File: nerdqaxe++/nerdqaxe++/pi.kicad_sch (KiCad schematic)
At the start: 20 parts, among them J5 Conn_01x12-Socket, J6 Conn_01x12-Socket, J7 Conn_01x12-Header, J8 Conn_01x12-Header, M1 Fan_4pin, M2 Fan_4pin, U30 T-Display-S3, U32 EMC2302-1, U33 TXU0102-DCU, U37 TMP1075, U38 TMP1075

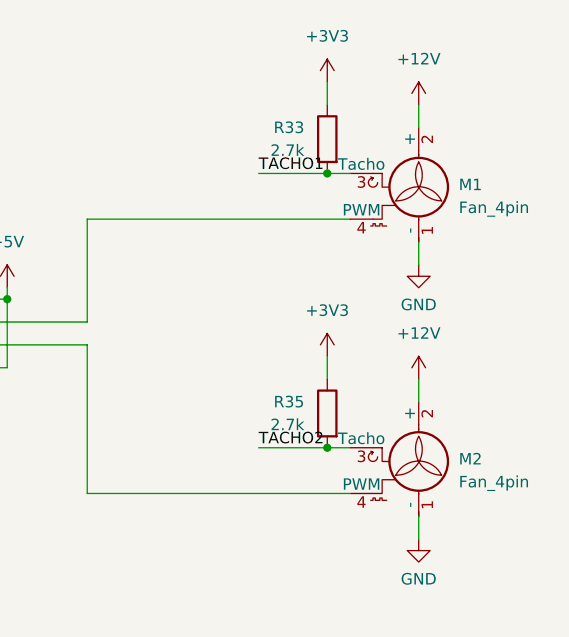
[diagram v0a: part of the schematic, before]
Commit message: removed solderjumpers on ++
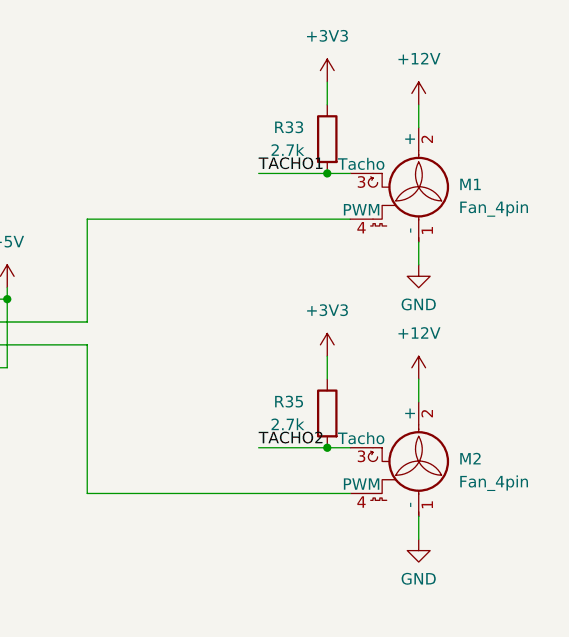
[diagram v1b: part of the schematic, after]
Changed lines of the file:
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@@
 (kicad_sch
-	(version 20231120)
+	(version 20250114)
 	(generator "eeschema")
-	(generator_version "8.0")
+	(generator_version "9.0")
 	(paper "A4")
+	(text "1x12 Socket for NerdQaxe+"
+		(exclude_from_sim no)
+		(at 29.21 179.07 0)
+		(effects
+			(font
+				(size 1.27 1.27)
+			)
+		)
+	)
+	(text "1x12 Pinheader for T-Display-S3"
+		(exclude_from_sim no)
+		(at 61.595 179.07 0)
+		(effects
+			(font
+				(size 1.27 1.27)
+			)
+		)
+	)
 	(junction
 		(at 220.345 131.445)
@@
 		)
 	)
-	(text "1x12 Socket for NerdQaxe+"
-		(exclude_from_sim no)
-		(at 29.21 179.07 0)
-		(effects
-			(font
-				(size 1.27 1.27)
-			)
-		)
-	)
-	(text "1x12 Pinheader for T-Display-S3"
-		(exclude_from_sim no)
-		(at 61.595 179.07 0)
-		(effects
-			(font
-				(size 1.27 1.27)
-			)
-		)
-	)
 	(label "SCL"
 		(at 201.295 53.975 0)
-		(fields_autoplaced yes)
 		(effects
 			(font
@@
 	(label "SDA"
 		(at 248.285 53.975 180)
-		(fields_autoplaced yes)
 		(effects
 			(font
@@
 	(label "SDA"
 		(at 139.065 128.905 180)
-		(fields_autoplaced yes)
 		(effects
 			(font
@@
 	(label "SCL"
 		(at 139.065 131.445 180)
-		(fields_autoplaced yes)
 		(effects
 			(font
@@
 	(label "TACHO1"
 		(at 174.625 139.065 0)
-		(fields_autoplaced yes)
 		(effects
 			(font
@@
 	(label "TACHO2"
 		(at 174.625 133.985 0)
-		(fields_autoplaced yes)
 		(effects
 			(font
@@
 	(label "TACHO2"
 		(at 248.285 147.955 0)
-		(fields_autoplaced yes)
 		(effects
 			(font
@@
 	(label "TACHO1"
 		(at 248.285 117.475 0)
-		(fields_autoplaced yes)
 		(effects
 			(font
@@
 		(shape bidirectional)
 		(at 154.305 76.835 0)
-		(fields_autoplaced yes)
 		(effects
 			(font
@@
 		(shape input)
 		(at 57.785 18.415 180)
-		(fields_autoplaced yes)
 		(effects
 			(font
@@
 		(shape output)
 		(at 97.79 79.375 180)
-		(fields_autoplaced yes)
 		(effects
 			(font
@@
 		(shape input)
 		(at 154.305 79.375 0)
-		(fields_autoplaced yes)
 		(effects
 			(font
@@
 		(shape input)
 		(at 103.505 99.695 180)
-		(fields_autoplaced yes)
 		(effects
 			(font
@@
 		(shape output)
 		(at 57.785 23.495 180)
-		(fields_autoplaced yes)
 		(effects
 			(font
@@
 		(shape output)
 		(at 154.305 74.295 0)
-		(fields_autoplaced yes)
 		(effects
 			(font
@@
 		(shape output)
 		(at 113.665 71.755 180)
-		(fields_autoplaced yes)
 		(effects
 			(font
@@
 		(shape input)
 		(at 57.785 20.955 180)
-		(fields_autoplaced yes)
 		(effects
 			(font
@@
 		(shape output)
 		(at 154.305 81.915 0)
-		(fields_autoplaced yes)
 		(effects
 			(font
@@
 		(shape output)
 		(at 110.49 86.995 180)
-		(fields_autoplaced yes)
 		(effects
 			(font
@@
 		(shape input)
 		(at 80.645 81.915 180)
-		(fields_autoplaced yes)
 		(effects
 			(font
@@
 		)
 	)
+	(embedded_fonts no)
 )

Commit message: rev5.1.1
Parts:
- added R16: 10k, Resistor_SMD:R_0805_2012Metric, symbol Device:R
- added R8, R9: 3.3k, Resistor_SMD:R_0805_2012Metric, symbol Device:R
- C102, C103, C87, C88, C96: Distributor (none) -> D; Manufacturer (none) -> C0805C104K5RACTU; OrderNr (none) -> 399-C0805C104K5RACTUCT-ND; temp-coefficient (none) -> X7R
- R33, R35: Distributor (none) -> D; Manufacturer (none) -> RMCF0805FT2K70; OrderNr (none) -> RMCF0805FT2K70CT-ND
- R36: Distributor (none) -> D; Manufacturer (none) -> RMCF0805FT10K0; OrderNr (none) -> RMCF0805FT10K0CT-ND
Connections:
- net +3V3: now also R8.1, R9.1
- net GND: now also R16.2
- net RESET: now also R16.1
- net SCL: now also R8.2
- net SDA: now also R9.2
